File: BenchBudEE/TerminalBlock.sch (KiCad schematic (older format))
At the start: 0 parts

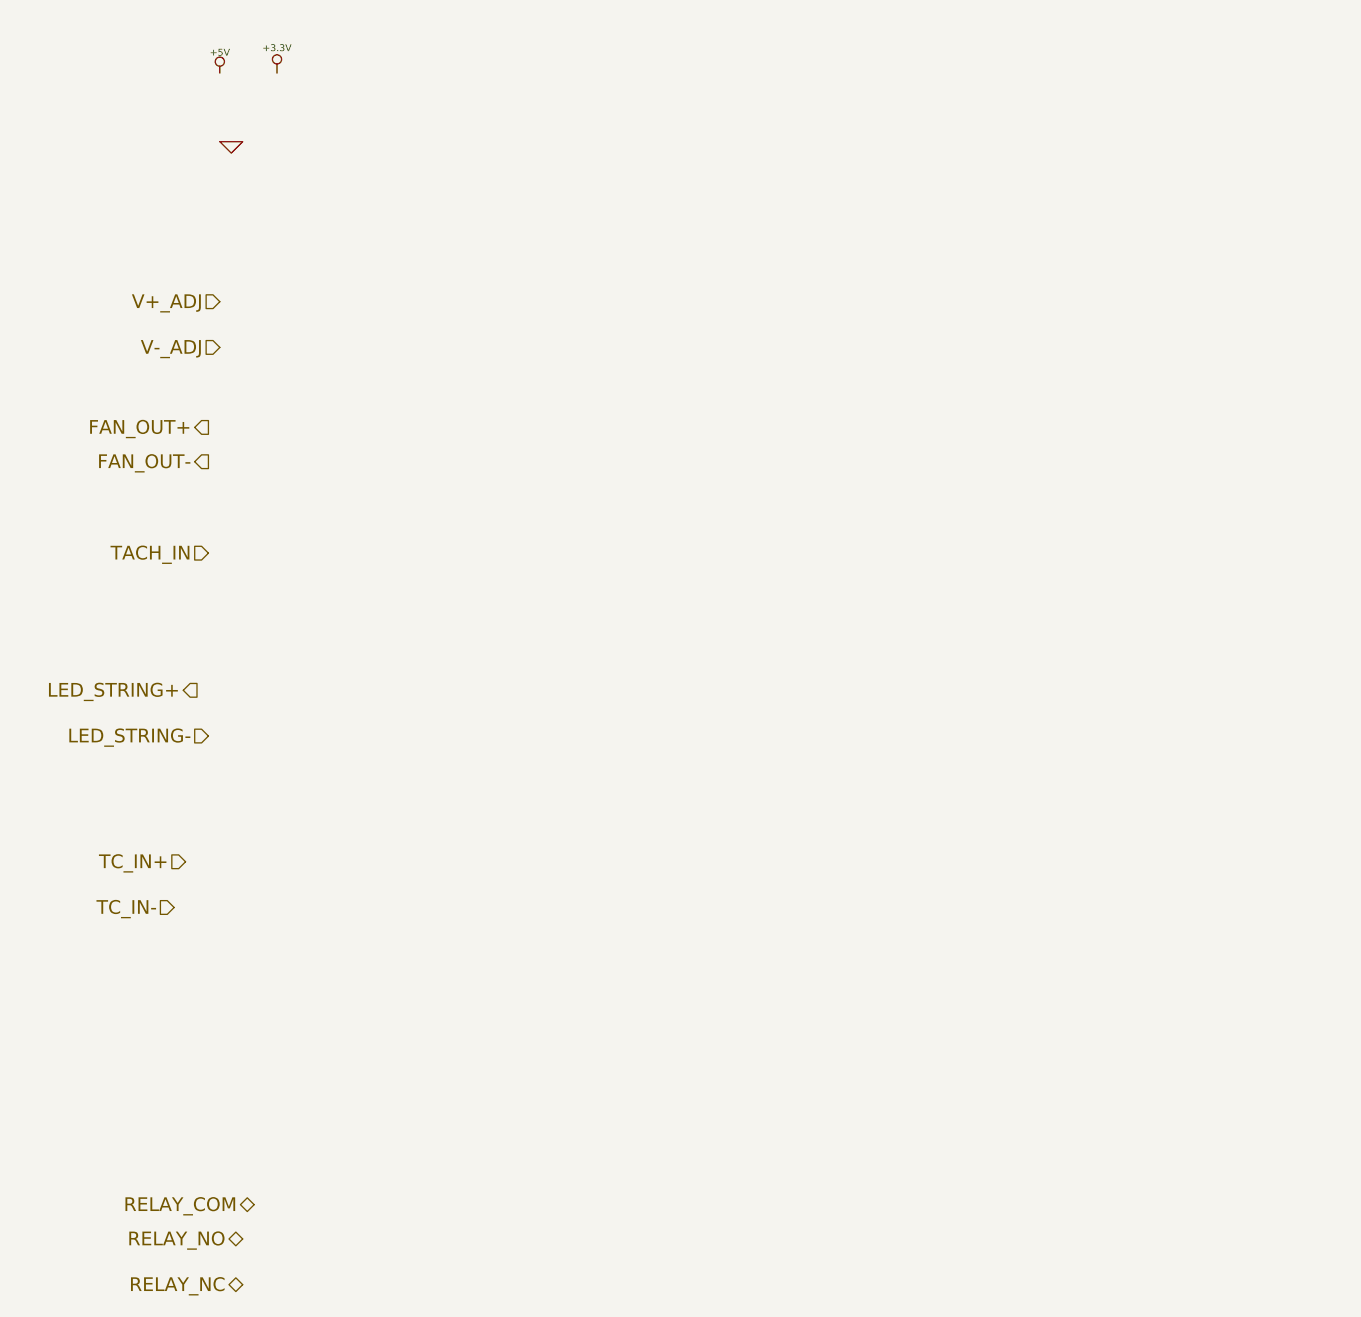
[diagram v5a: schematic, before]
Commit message: Arduino module associated + roughly placed.
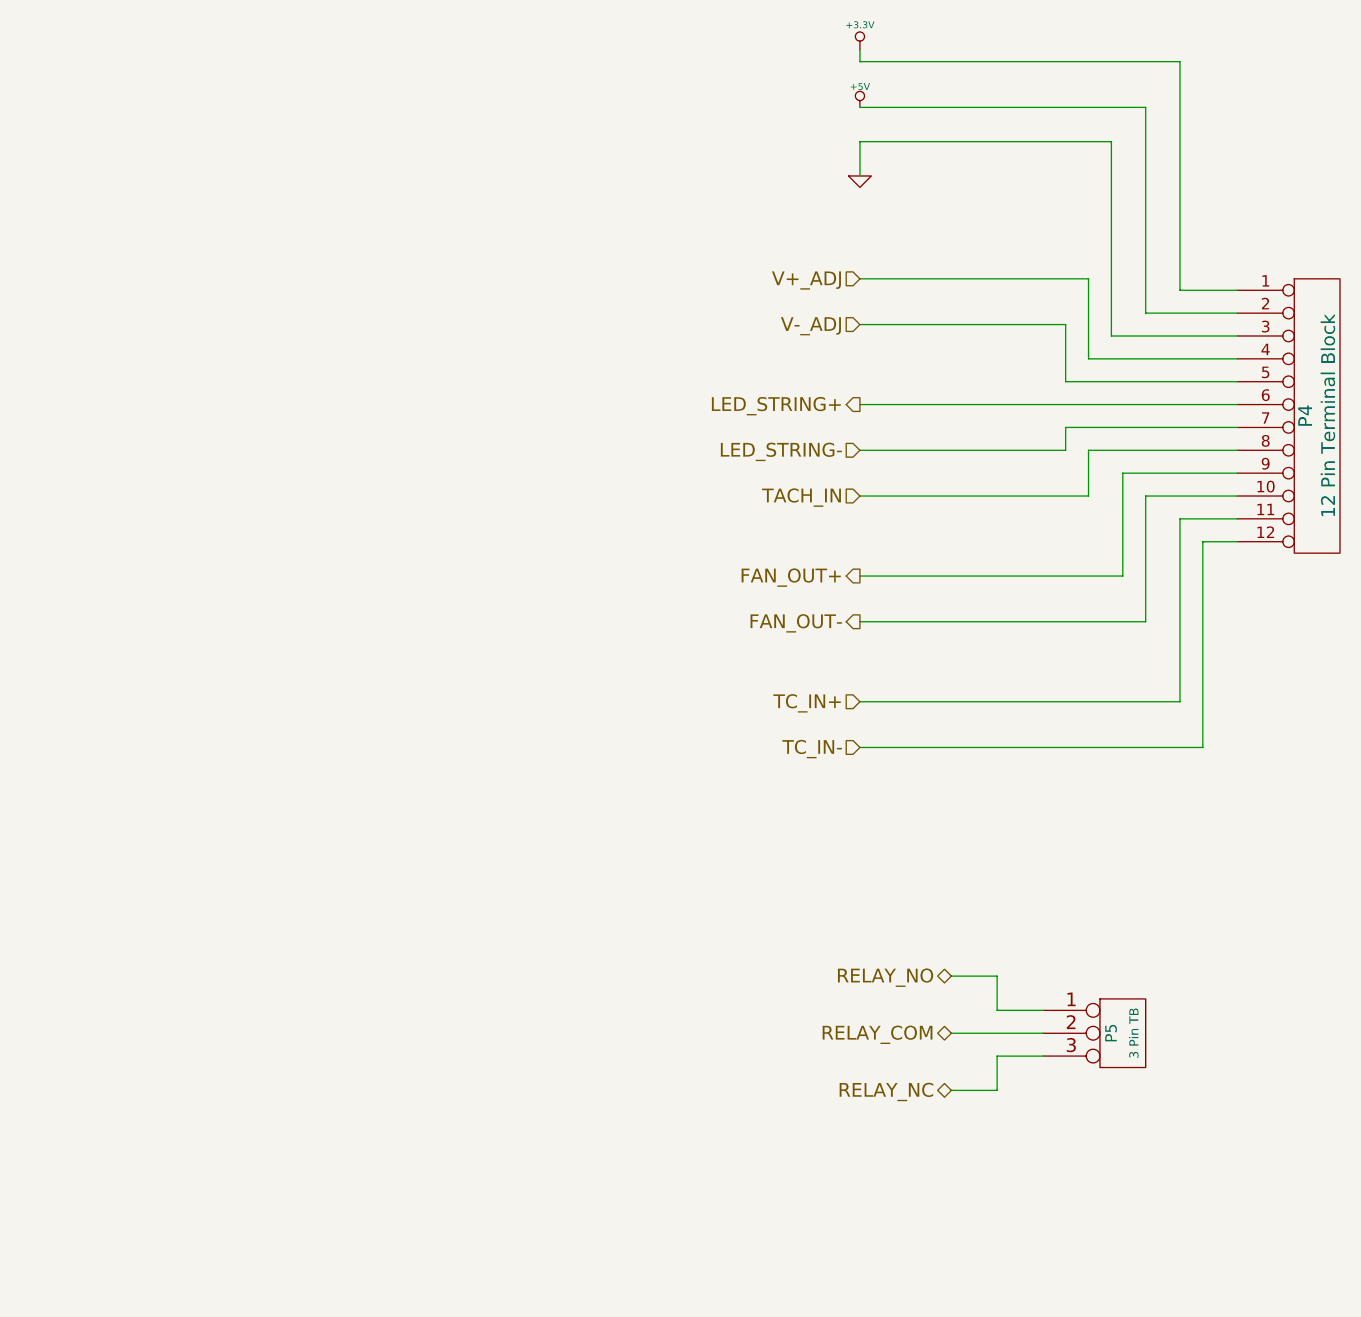
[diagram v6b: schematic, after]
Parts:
- added P4: 12 Pin Terminal Block, symbol CONN_12
- added P5: 3 Pin TB, symbol CONN_3
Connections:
- net +3.3V: now also P4.1 (P1)
- net +5V: now also P4.2 (P2)
- net FAN_OUT+: now also P4.9 (P9)
- net FAN_OUT-: now also P4.10 (P10)
- net GND: now also P4.3 (P3)
- net LED_STRING+: now also P4.6 (P6)
- net LED_STRING-: now also P4.7 (P7)
- net RELAY_COM: now also P5.2 (PM)
- net RELAY_NC: now also P5.3 (P3)
- net RELAY_NO: now also P5.1 (P1)
- net TACH_IN: now also P4.8 (P8)
- net TC_IN+: now also P4.11 (P11)
- net TC_IN-: now also P4.12 (P12)
- net V+_ADJ: now also P4.4 (P4)
- net V-_ADJ: now also P4.5 (P5)
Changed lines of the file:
@@
 $Descr A4 11693 8268
 encoding utf-8
-Sheet 5 9
+Sheet 4 9
 Title ""
-Date "20 feb 2014"
+Date "23 feb 2014"
 Rev ""
 Comp ""
@@
 Comment4 ""
 $EndDescr
-Text HLabel 2050 2350 0    60   Input ~ 0
+Text HLabel 4850 2250 0    60   Input ~ 0
 V+_ADJ
-Text HLabel 2050 2550 0    60   Input ~ 0
+Text HLabel 4850 2450 0    60   Input ~ 0
 V-_ADJ
-Text HLabel 2000 2900 0    60   Output ~ 0
+Text HLabel 4850 3550 0    60   Output ~ 0
 FAN_OUT+
-Text HLabel 2000 3050 0    60   Output ~ 0
+Text HLabel 4850 3750 0    60   Output ~ 0
 FAN_OUT-
-Text HLabel 2000 3450 0    60   Input ~ 0
+Text HLabel 4850 3200 0    60   Input ~ 0
 TACH_IN
-Text HLabel 1950 4050 0    60   Output ~ 0
+Text HLabel 4850 2800 0    60   Output ~ 0
 LED_STRING+
-Text HLabel 2000 4250 0    60   Input ~ 0
+Text HLabel 4850 3000 0    60   Input ~ 0
 LED_STRING-
-Text HLabel 1900 4800 0    60   Input ~ 0
+Text HLabel 4850 4100 0    60   Input ~ 0
 TC_IN+
-Text HLabel 1850 5000 0    60   Input ~ 0
+Text HLabel 4850 4300 0    60   Input ~ 0
 TC_IN-
-Text HLabel 2200 6300 0    60   BiDi ~ 0
+Text HLabel 5250 5550 0    60   BiDi ~ 0
 RELAY_COM
-Text HLabel 2150 6450 0    60   BiDi ~ 0
+Text HLabel 5250 5300 0    60   BiDi ~ 0
 RELAY_NO
-Text HLabel 2150 6650 0    60   BiDi ~ 0
+Text HLabel 5250 5800 0    60   BiDi ~ 0
 RELAY_NC
 $Comp
 L +5V #PWR07
 U 1 1 52F4C602
-P 2050 1350
-F 0 "#PWR07" H 2050 1440 20  0001 C CNN
-F 1 "+5V" H 2050 1440 30  0000 C CNN
-F 2 "" H 2050 1350 60  0000 C CNN
-F 3 "" H 2050 1350 60  0000 C CNN
-	1    2050 1350
+P 4850 1500
+F 0 "#PWR07" H 4850 1590 20  0001 C CNN
+F 1 "+5V" H 4850 1590 30  0000 C CNN
+F 2 "" H 4850 1500 60  0000 C CNN
+F 3 "" H 4850 1500 60  0000 C CNN
+	1    4850 1500
 	1    0    0    -1
 $EndComp
@@
 L +3.3V #PWR08
 U 1 1 52F4C611
-P 2300 1350
-F 0 "#PWR08" H 2300 1310 30  0001 C CNN
-F 1 "+3.3V" H 2300 1460 30  0000 C CNN
-F 2 "" H 2300 1350 60  0000 C CNN
-F 3 "" H 2300 1350 60  0000 C CNN
-	1    2300 1350
+P 4850 1250
+F 0 "#PWR08" H 4850 1210 30  0001 C CNN
+F 1 "+3.3V" H 4850 1360 30  0000 C CNN
+F 2 "" H 4850 1250 60  0000 C CNN
+F 3 "" H 4850 1250 60  0000 C CNN
+	1    4850 1250
 	1    0    0    -1
 $EndComp
@@
 L GND #PWR09
 U 1 1 52F4C620
-P 2100 1650
-F 0 "#PWR09" H 2100 1650 30  0001 C CNN
-F 1 "GND" H 2100 1580 30  0001 C CNN
-F 2 "" H 2100 1650 60  0000 C CNN
-F 3 "" H 2100 1650 60  0000 C CNN
-	1    2100 1650
+P 4850 1800
+F 0 "#PWR09" H 4850 1800 30  0001 C CNN
+F 1 "GND" H 4850 1730 30  0001 C CNN
+F 2 "" H 4850 1800 60  0000 C CNN
+F 3 "" H 4850 1800 60  0000 C CNN
+	1    4850 1800
 	1    0    0    -1
 $EndComp
+$Comp
+L CONN_12 P4
+U 1 1 5307A0FF
+P 6850 2850
+F 0 "P4" V 6800 2850 60  0000 C CNN
+F 1 "12 Pin Terminal Block" V 6900 2850 60  0000 C CNN
+F 2 "" H 6850 2850 60  0000 C CNN
+F 3 "http://www.on-shore.com/sites/default/files/manuals/OSTTEXX0164.pdf" H 6850 2850 60  0001 C CNN
+F 4 "On Shore Technology Inc" H 6850 2850 60  0001 C CNN "MFG Name"
+F 5 "OSTTE120104" H 6850 2850 60  0001 C CNN "MFG Part Number"
+F 6 "DIgiKey" H 6850 2850 60  0001 C CNN "Distributor"
+F 7 "ED2737-ND" H 6850 2850 60  0001 C CNN "Distributor Part Number"
+F 8 "http://www.digikey.com/product-detail/en/OSTTE120104/ED2737-ND/2351813" H 6850 2850 60  0001 C CNN "Distributor Part Link"
+	1    6850 2850
+	1    0    0    -1
+$EndComp
+Wire Wire Line
+	6500 2300 6250 2300
+Wire Wire Line
+	6250 2300 6250 1300
+Wire Wire Line
+	6250 1300 4850 1300
+Wire Wire Line
+	4850 1300 4850 1250
+Wire Wire Line
+	4850 1500 6100 1500
+Wire Wire Line
+	6100 1500 6100 2400
+Wire Wire Line
+	6100 2400 6500 2400
+Wire Wire Line
+	4850 1800 4850 1650
+Wire Wire Line
+	4850 1650 5950 1650
+Wire Wire Line
+	5950 1650 5950 2500
+Wire Wire Line
+	5950 2500 6500 2500
+Wire Wire Line
+	4850 2250 5850 2250
+Wire Wire Line
+	5850 2250 5850 2600
+Wire Wire Line
+	5850 2600 6500 2600
+Wire Wire Line
+	4850 2450 5750 2450
+Wire Wire Line
+	5750 2450 5750 2700
+Wire Wire Line
+	5750 2700 6500 2700
+Wire Wire Line
+	4850 2800 6500 2800
+Wire Wire Line
+	4850 3000 5750 3000
+Wire Wire Line
+	5750 3000 5750 2900
+Wire Wire Line
+	5750 2900 6500 2900
+Wire Wire Line
+	4850 3200 5850 3200
+Wire Wire Line
+	5850 3200 5850 3000
+Wire Wire Line
+	5850 3000 6500 3000
+Wire Wire Line
+	4850 3550 6000 3550
+Wire Wire Line
+	6000 3550 6000 3100
+Wire Wire Line
+	6000 3100 6500 3100
+Wire Wire Line
+	6500 3200 6100 3200
+Wire Wire Line
+	6100 3200 6100 3750
+Wire Wire Line
+	6100 3750 4850 3750
+Wire Wire Line
+	6500 3300 6250 3300
+Wire Wire Line
+	6250 3300 6250 4100
+Wire Wire Line
+	6250 4100 4850 4100
+Wire Wire Line
+	4850 4300 6350 4300
+Wire Wire Line
+	6350 4300 6350 3400
+Wire Wire Line
+	6350 3400 6500 3400
+$Comp
+L CONN_3 P5
+U 1 1 5307A296
+P 6000 5550
+F 0 "P5" V 5950 5550 50  0000 C CNN
+F 1 "3 Pin TB" V 6050 5550 40  0000 C CNN
+F 2 "" H 6000 5550 60  0000 C CNN
+F 3 "http://media.digikey.com/pdf/Data%20Sheets/Phoenix%20Contact%20PDFs/COMBICON%20Compact%205.0mm%20Series.pdf" H 6000 5550 60  0001 C CNN
+F 4 "Phoenix Contact" H 6000 5550 60  0001 C CNN "MFG Name"
+F 5 "1935174" H 6000 5550 60  0001 C CNN "MFG Part Number"
+F 6 "DigiKey" H 6000 5550 60  0001 C CNN "Distributor"
+F 7 "277-1578-ND" H 6000 5550 60  0001 C CNN "Distributor Part Number"
+F 8 "http://www.digikey.com/product-detail/en/1935174/277-1578-ND/568615" H 6000 5550 60  0001 C CNN "Distributor Part Link"
+	1    6000 5550
+	1    0    0    -1
+$EndComp
+Wire Wire Line
+	5250 5550 5650 5550
+Wire Wire Line
+	5650 5450 5450 5450
+Wire Wire Line
+	5450 5450 5450 5300
+Wire Wire Line
+	5450 5300 5250 5300
+Wire Wire Line
+	5250 5800 5450 5800
+Wire Wire Line
+	5450 5800 5450 5650
+Wire Wire Line
+	5450 5650 5650 5650
 $EndSCHEMATC
